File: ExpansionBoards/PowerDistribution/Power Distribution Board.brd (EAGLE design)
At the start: 160 x 73.2 mm, 31 parts, among them J1 216571-2002, J10 640445-6, J11 640445-6, J12 640445-2, J13 640445-5, J14 640445-3, J15 216571-2003, J16 640445-8, J2 216571-2005, J3 216571-2005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

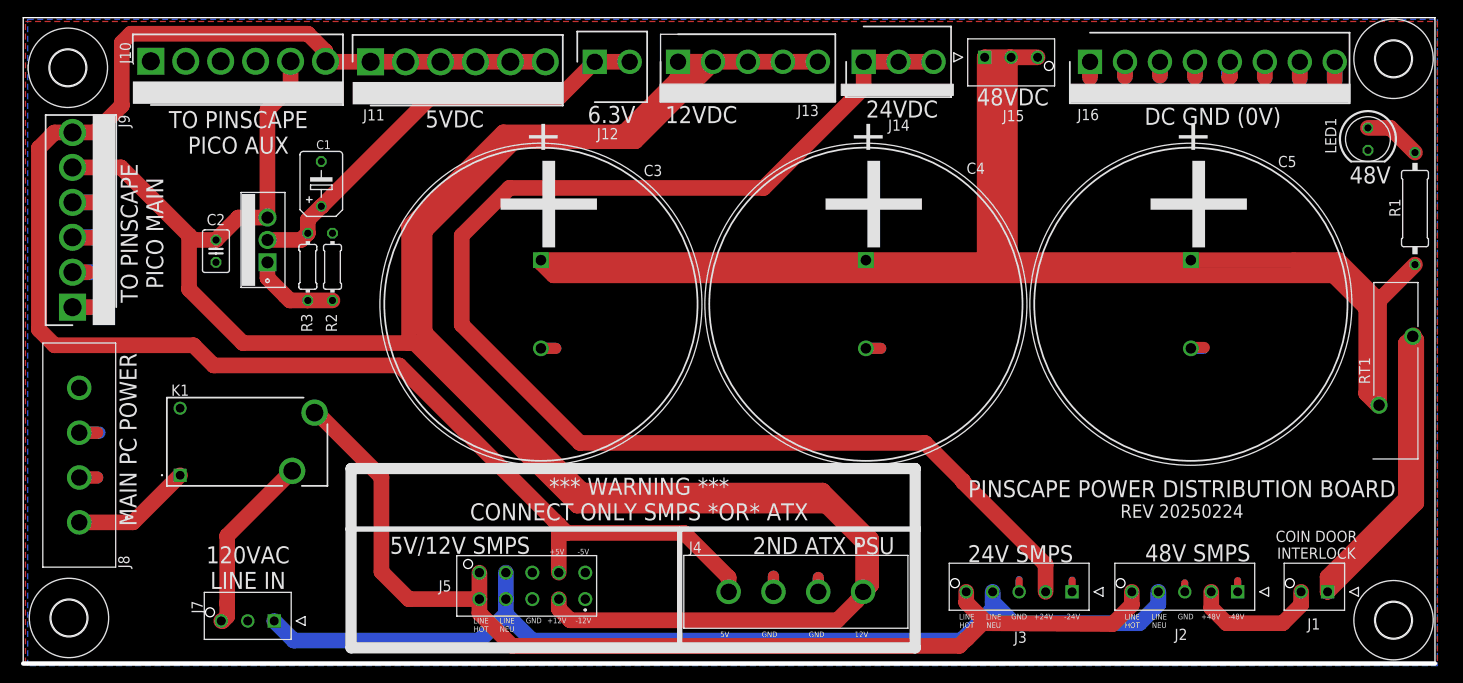
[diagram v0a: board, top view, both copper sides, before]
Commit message: exp board: power distro: add relay coil diode
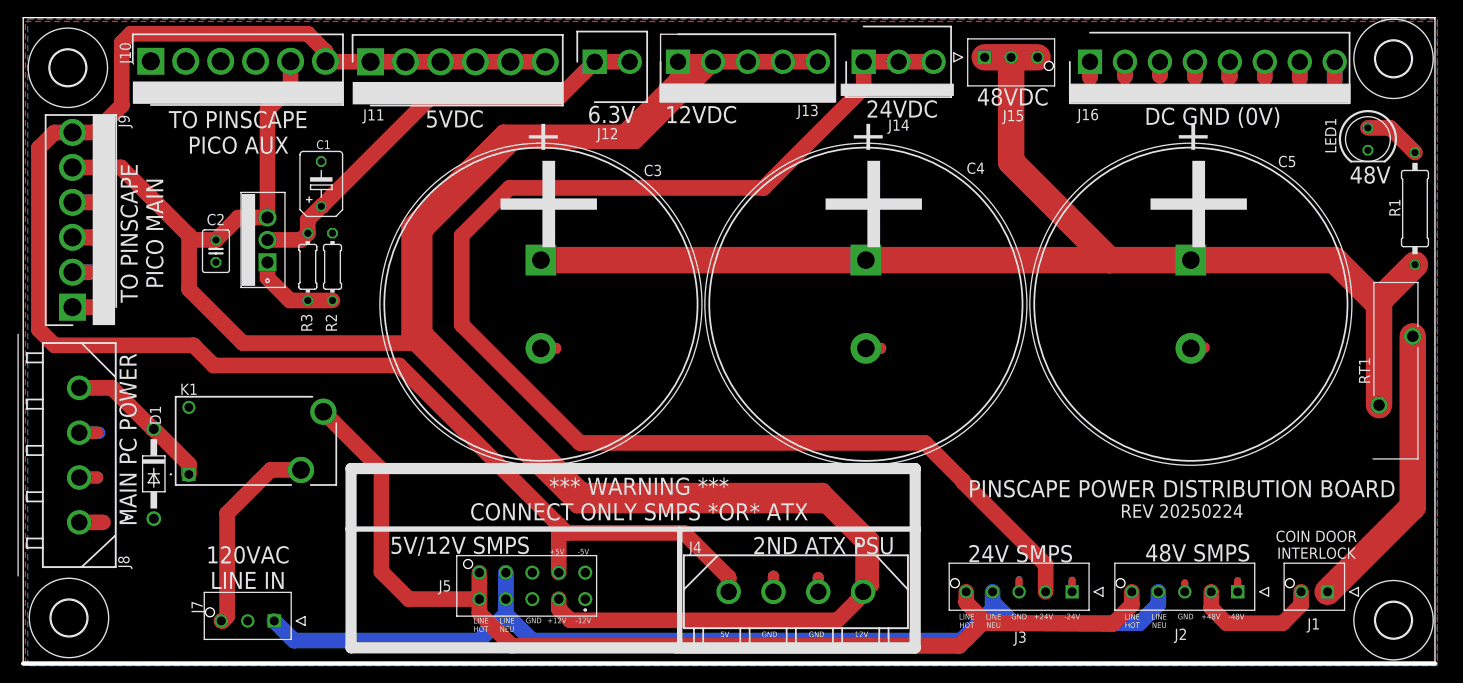
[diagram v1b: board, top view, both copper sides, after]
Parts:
- added D1: 1N4007, diode:DO41-10
- moved K1 1.00 mm to (18.8, 21.4)
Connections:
- net 12VPC: no longer K1.1
- net 5VPC: now also D1.C, K1.1
- net GND: now also D1.A
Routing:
- net 48V: track 297.9 -> 148.3 mm
- net N$2: track 66.4 -> 33.0 mm
- net 5VPC: track 0.00 -> 17.2 mm
- net 12VPC: track 13.6 -> 2.70 mm
- net LINE_HOT_IN: track 20.4 -> 23.0 mm
